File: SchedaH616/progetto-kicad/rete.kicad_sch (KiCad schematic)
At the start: 43 parts, among them J501 HR911130C, U501 RTL8211F-CG, U502 25AA02E48T-I/OT, Y501 25MHz

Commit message: SchedaH616: RK3568 + RK809-5 + TCS4525 + DDR4, placement 50x70
- SoC Allwinner H616 -> Rockchip RK3568 (FCBGA636L, LCSC C2938930): ball map dal pinout
  Rockchip V1.1, verificata sulla tabella 2-1 del datasheet V1.2 (636/636); footprint
  generato (gen_fp.py), confrontato con EasyEDA C2938930
- PMIC AXP313A -> RK809-5 (C2939628) come Rockchip AIoT REF V1.1 / ROCK 3A; TCS4525 per
  VDD_CPU su I2C0 (0x1C); BUCK4 su VDD_NPU (sull'RK809-5 parte spento: non puo' fare il 3.3 V)
- LPDDR4 -> DDR4 x16 K4AAG165WA-BCWE (C2920140) sul canale A, point-to-point, niente VTT,
  VPP da AP2112K-2.5, ZQ 240R, DDR_RZQ del SoC 120R (Hardware Design Guide)
- eMMC su EMMC 8 bit (VCCIO2 1.8 V), microSD su SDMMC0, AP6256 su SDMMC2 + UART8,
  RTL8211F su GMAC0 RGMII (22R TX al SoC e RX al PHY), console UART2_M0, USB-C su OTG0
- Recovery su SARADC_VIN0, reset sulla rete RESETn; TCA6416A tolto
- Bus MIKILAB: BUS_POWER su SPI3_M1, MAIN su SPI2_M1 (CS del DAC su cs-gpios)
- progetto rinominato SchedaRK3568, libreria di progetto Scheda; script portabili Linux/macOS
- ERC 0, parita' 0, DRC 0 (solo collegamenti da fare); placement 439/439

Co-Authored-By: Claude Opus 5.5 (1M context) <noreply@anthropic.com>
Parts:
- removed J501: HR911130C, H616:RJ45-TH_HR911130C, symbol H616:HR911130C
- removed U501: RTL8211F-CG, Package_DFN_QFN:QFN-40-1EP_5x5mm_P0.4mm_EP3.6x3.6mm, symbol H616:RTL8211F-CG
- removed U502: 25AA02E48T-I/OT, Package_TO_SOT_SMD:SOT-23-6, symbol H616:25AA02E48
- added J501: HR911130C, Scheda:RJ45-TH_HR911130C, symbol Scheda:HR911130C
- added R524, R525, R526, R527, R528, R529: 22R, Resistor_SMD:R_0402_1005Metric, symbol Device:R
- added U501: RTL8211F-CG, Package_DFN_QFN:QFN-40-1EP_5x5mm_P0.4mm_EP3.6x3.6mm, symbol Scheda:RTL8211F-CG
- added U502: 25AA02E48T-I/OT, Package_TO_SOT_SMD:SOT-23-6, symbol Scheda:25AA02E48
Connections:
- net ETH_CT: now also J501.P1 (CT)
- net ETH_LED1_A: now also J501.11 (LED_G_A)
- net ETH_LED2_A: now also J501.14 (LED_Y_A)
- net GND_D: now also J501.12 (LED_G_K), J501.13 (LED_Y_K), J501.P10 (BOB_SMITH), J501.SHIELD0 (SHIELD), J501.SHIELD1 (SHIELD), U501.41 (EPAD_GND), U502.2 (VSS)
- net MDI0_N: now also J501.P3 (MDI0-), U501.2 (MDIN0)
- net MDI0_P: now also J501.P2 (MDI0+), U501.1 (MDIP0)
- net MDI1_N: now also J501.P7 (MDI1-), U501.5 (MDIN1)
- net MDI1_P: now also J501.P4 (MDI1+), U501.4 (MDIP1)
- net MDI2_N: now also J501.P6 (MDI2-), U501.7 (MDIN2)
- net MDI2_P: now also J501.P5 (MDI2+), U501.6 (MDIP2)
- net MDI3_N: now also J501.P9 (MDI3-), U501.10 (MDIN3)
- net MDI3_P: now also J501.P8 (MDI3+), U501.9 (MDIP3)
- net PHY_CLKOUT: now also U501.35 (CLKOUT)
- net PHY_EE_CS_N: now also U502.5 (~{CS})
- net PHY_INT_N: now also U501.31 (INTB/PMEB)
- net PHY_LED0: now also U501.32 (LED0/CFG_EXT)
- net PHY_LED1: now also U501.33 (LED1/CFG_LDO0)
- net PHY_LED2: now also U501.34 (LED2/CFG_LDO1)
- net PHY_MDC: now also U501.13 (MDC)
- net PHY_MDIO: now also U501.14 (MDIO)
- net PHY_REG_OUT: now also U501.30 (REG_OUT)
- net PHY_RSET: now also U501.39 (RSET)
- net PHY_RST_N: now also U501.12 (PHYRSTB)
- net PHY_TXCTL_P: now also U501.19 (TXCTL)
- net PHY_TXC_P: now also U501.20 (TXC)
- net PHY_TXD0_P: now also U501.18 (TXD0)
- net PHY_TXD1_P: now also U501.17 (TXD1)
- net PHY_TXD2_P: now also U501.16 (TXD2)
- net PHY_TXD3_P: now also U501.15 (TXD3)
- net PHY_VDD10: now also U501.21 (DVDD10), U501.3 (AVDD10), U501.38 (AVDD10), U501.8 (AVDD10)
- net PHY_XI: now also U501.36 (XTAL_IN)
- net PHY_XO: now also U501.37 (XTAL_OUT)
- net RGMII_RXCK: now also R524.2; no longer R508.1
- net RGMII_RXCTL: now also R529.2; no longer R509.1
- net RGMII_RXD0: now also R525.2; no longer R512.2
- net RGMII_RXD1: now also R526.2; no longer R511.2
- net RGMII_RXD2: now also R527.2; no longer R510.1
- net RGMII_RXD3: now also R528.2; no longer R507.2
- net 3V3_PERI renamed VCC_3V3
- net VCC_3V3: now also U501.11 (AVDD33), U501.28 (DVDD_RG), U501.29 (DVDD33), U501.40 (AVDD33), U502.6 (VCC)
- new net PHY_RXCTL_P: R509.1, R529.1, U501.26 (RXCTL/PHYAD2)
- new net PHY_RXC_P: R508.1, R524.1, U501.27 (RXC/PHYAD1)
- new net PHY_RXD0_P: R512.2, R525.1, U501.25 (RXD0/RXDLY)
- new net PHY_RXD1_P: R511.2, R526.1, U501.24 (RXD1/TXDLY)
- new net PHY_RXD2_P: R510.1, R527.1, U501.23 (RXD2/PLLOFF)
- new net PHY_RXD3_P: R507.2, R528.1, U501.22 (RXD3/PHYAD0)
- new net SPI2_CLK: U502.1 (SCK)
- new net SPI2_MISO: U502.4 (SO)
- new net SPI2_MOSI: U502.3 (SI)
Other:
- note added: "22R serie vicino al SoC su TXC, TXD0-3, TXCTL (MAC -> PHY) e vicino al PHY su RXC, RXD0-3, RXCTL (Hardware Design Guide RK3568, tabella 2-42)."
- note added: "EEPROM MAC 25AA02E48 (EUI-48 per la MAC del GMAC0) su SPI2 locale (prima dei 33R verso il bus MAIN), CS1 hardware di SPI2 (GPIO2_D4) con 10k a VCC_3V3."
- note added: "MDIO 1.5k a 3.3 V, INT 4.7k, PHYRSTB 10k + 100 nF (il PHY esce dal reset da solo, Linux puo' ripeterlo da GPIO3_D7). RSET 2.49k 1%."
- note added: "R520 DNP: CLKOUT 125 MHz verso GMAC0_MCLKINOUT (GPIO2_C2), non usato di default. PHY_RST_N su GPIO3_D7, PHY_INT_N su GPIO4_A0."
- note added: "RETE: PHY Realtek RTL8211F-CG (datasheet rev. 1.7) su GMAC0 RGMII dell'RK3568 (VCCIO4 3.3 V), alimentato da VCC_3V3 (SWOUT1). Serie 5xx. Net RGMII_*/PHY_* globali verso il foglio CPU."
- note removed: "22R serie vicino al SoC su TXC, TXD0-3, TXCTL (MAC -> PHY). RX senza serie (sorgente PHY)."
- note removed: "EEPROM MAC 25AA02E48 (EUI-48 per la MAC dell'EMAC0) su SPI1 locale (prima dei 33R verso il bus), CS dall'espansore P16 con 10k a 3V3_PERI (deselezionata al reset)."
- note removed: "MDIO 1.5k a 3.3 V, INT 4.7k, PHYRSTB 10k + 100 nF (il PHY esce dal reset da solo, Linux puo' ripeterlo dall'espansore). RSET 2.49k 1%."
- note removed: "R520 DNP: CLKOUT 125 MHz verso RGMII_CLKIN (PI13), non usato di default. PHY_RST_N e PHY_INT_N passano dall'espansore TCA6416A (foglio CPU)."
- note removed: "RETE: PHY Realtek RTL8211F-CG (datasheet rev. 1.7) su RGMII EMAC0 banco PI (VCC_PI 3.3 V). Serie 5xx. Net RGMII_*/PHY_* globali verso il foglio CPU."

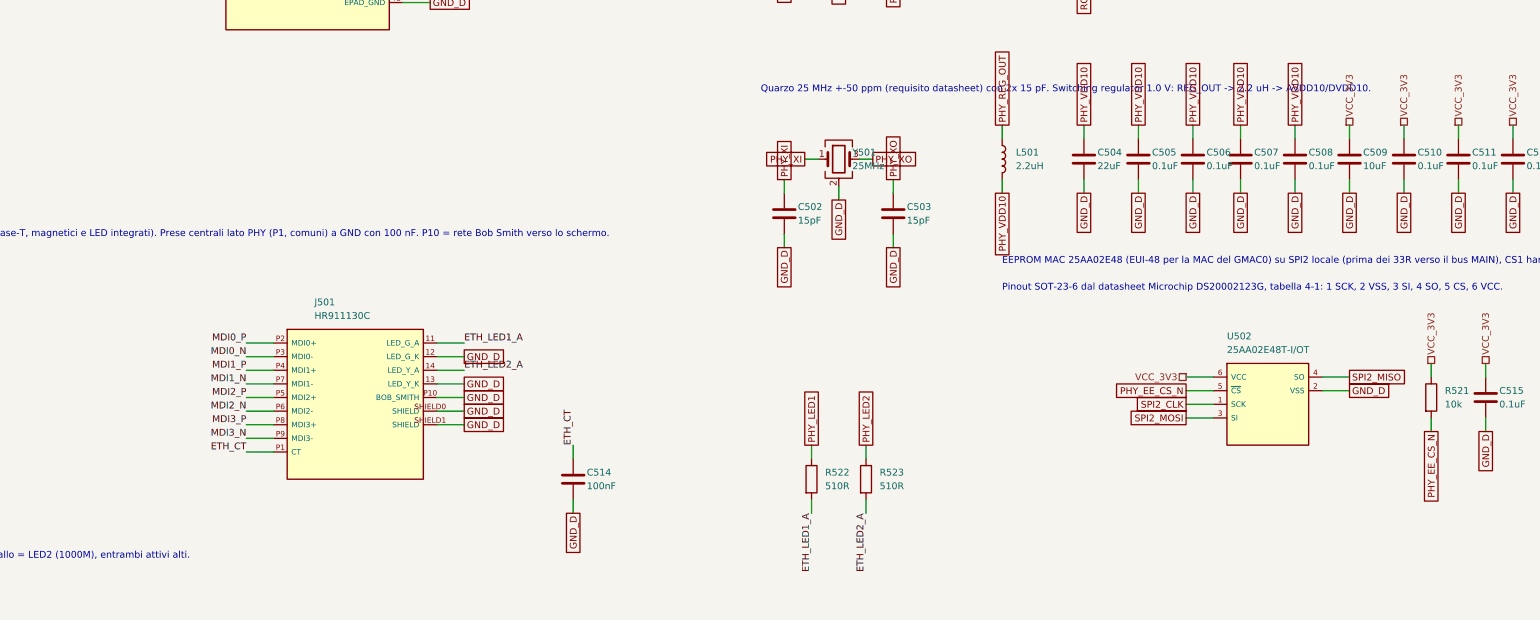
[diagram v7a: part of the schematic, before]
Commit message: SchedaH616: componenti specifici dalla libreria MIKILAB
- simbolo e footprint MIKILAB per RK809-5, TCS4525, K4AAG165WA-BCWE, FEMDNN064G-C9A61,
  AP2112K-1.8TRG1, TPS56637RPAR, TPS2121RUXR, SY6280AAC, TPS563201DDCR, TPS2553DBVR,
  TYPE-C-31-M-12, FH12-30S-0.5SH, FPC-05F-28PH20, HR911130C, 25AA02E48T-I/OT, DM3AT-SF-PEJM5;
  simbolo MIKILAB per l'AP6256
- restano nella libreria di progetto: RK3568 (pad EasyEDA da 0.35 mm, niente fanout 5/5 mil),
  simbolo RTL8211F (quello MIKILAB ha pin di alimentazione nascosti), footprint AP6256 LGA-47,
  portapila BS-12; motivazioni in docs/scelte-progetto.md
- kilib.mik() carica simboli e footprint dalla libreria (variabile MIKILAB); matrice ERC:
  pin unspecified dei simboli EasyEDA OK
- netlist identica a 4ca35fc (439 componenti, 314 net); ERC 0, parita' 0, DRC 0 (solo
  collegamenti da fare); footprint corretti nella libreria MIKILAB 8b990c4

Co-Authored-By: Claude Opus 5.5 (1M context) <noreply@anthropic.com>
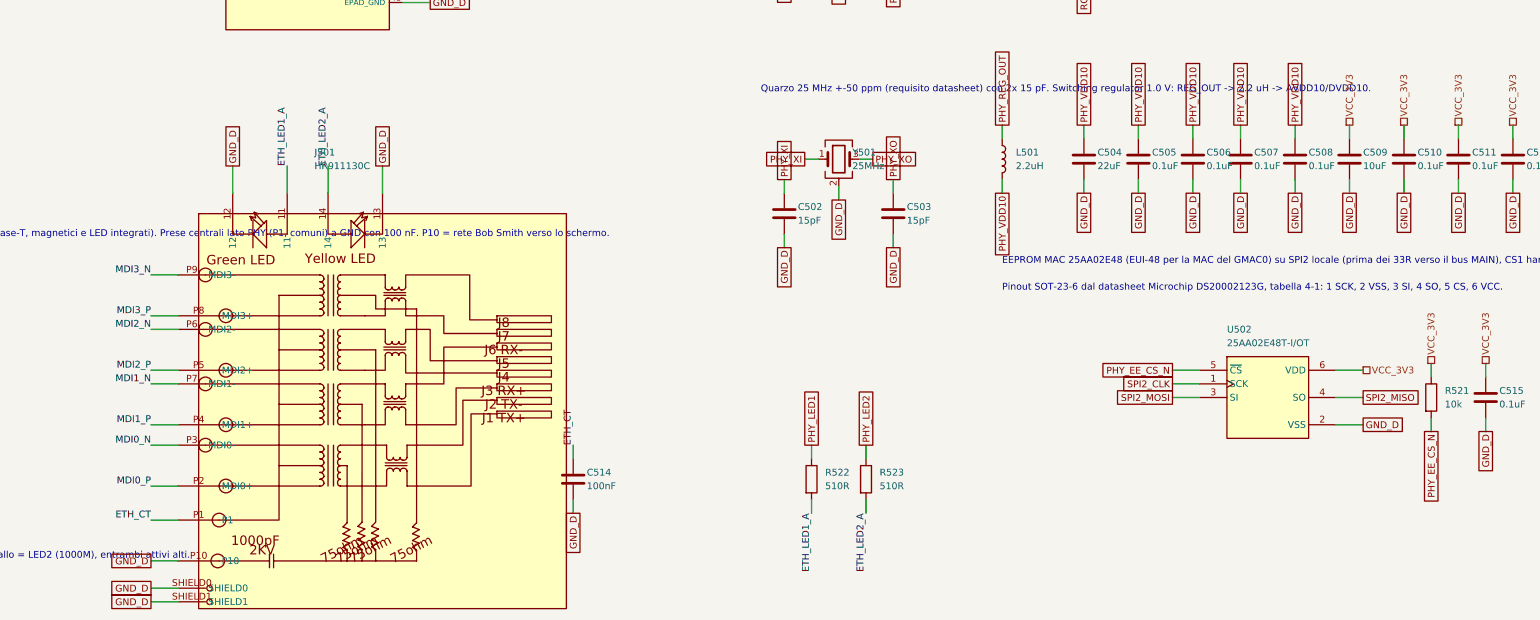
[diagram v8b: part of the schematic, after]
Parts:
- removed J501: HR911130C, Scheda:RJ45-TH_HR911130C, symbol Scheda:HR911130C
- removed U502: 25AA02E48T-I/OT, Package_TO_SOT_SMD:SOT-23-6, symbol Scheda:25AA02E48
- added J501: HR911130C, MIKILAB_HR911130C:RJ45-TH_HR911130C, symbol MIKILAB_HR911130C:HR911130C
- added U502: 25AA02E48T-I/OT, MIKILAB_25AA02E48T_I_OT:SOT-23-6_L2.9-W1.6-P0.95-LS2.8-BR, symbol MIKILAB_25AA02E48T_I_OT:25AA02E48T-I_OT
- U501: footprint Package_DFN_QFN:QFN-40-1EP_5x5mm_P0.4mm_EP3.6x3.6mm -> MIKILAB_RTL8211F_CG:QFN40P500X500X90-41N
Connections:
- net ETH_CT: now also J501.P1
- net ETH_LED1_A: now also J501.11
- net ETH_LED2_A: now also J501.14
- net GND_D: now also J501.12, J501.13, J501.P10, J501.SHIELD0, J501.SHIELD1, U502.2 (VSS)
- net MDI0_N: now also J501.P3 (MDI0-)
- net MDI0_P: now also J501.P2 (MDI0+)
- net MDI1_N: now also J501.P7 (MDI1-)
- net MDI1_P: now also J501.P4 (MDI1+)
- net MDI2_N: now also J501.P6 (MDI2-)
- net MDI2_P: now also J501.P5 (MDI2+)
- net MDI3_N: now also J501.P9 (MDI3-)
- net MDI3_P: now also J501.P8 (MDI3+)
- net PHY_EE_CS_N: now also U502.5 (~{CS})
- net SPI2_CLK: now also U502.1 (SCK)
- net SPI2_MISO: now also U502.4 (SO)
- net SPI2_MOSI: now also U502.3 (SI)
- net VCC_3V3: now also U502.6 (VDD)
